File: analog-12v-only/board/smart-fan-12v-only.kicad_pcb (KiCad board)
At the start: 2 copper layers, 62.2 x 41.3 mm, 30 parts, among them J1 KTY81/120, J2 12V_PWR, J3 12V_In, J4 FAN_Out, J5 FAN_Out, Q1 2N3904, Q2 FQP27P06, U1 LM358, U3 NE555P

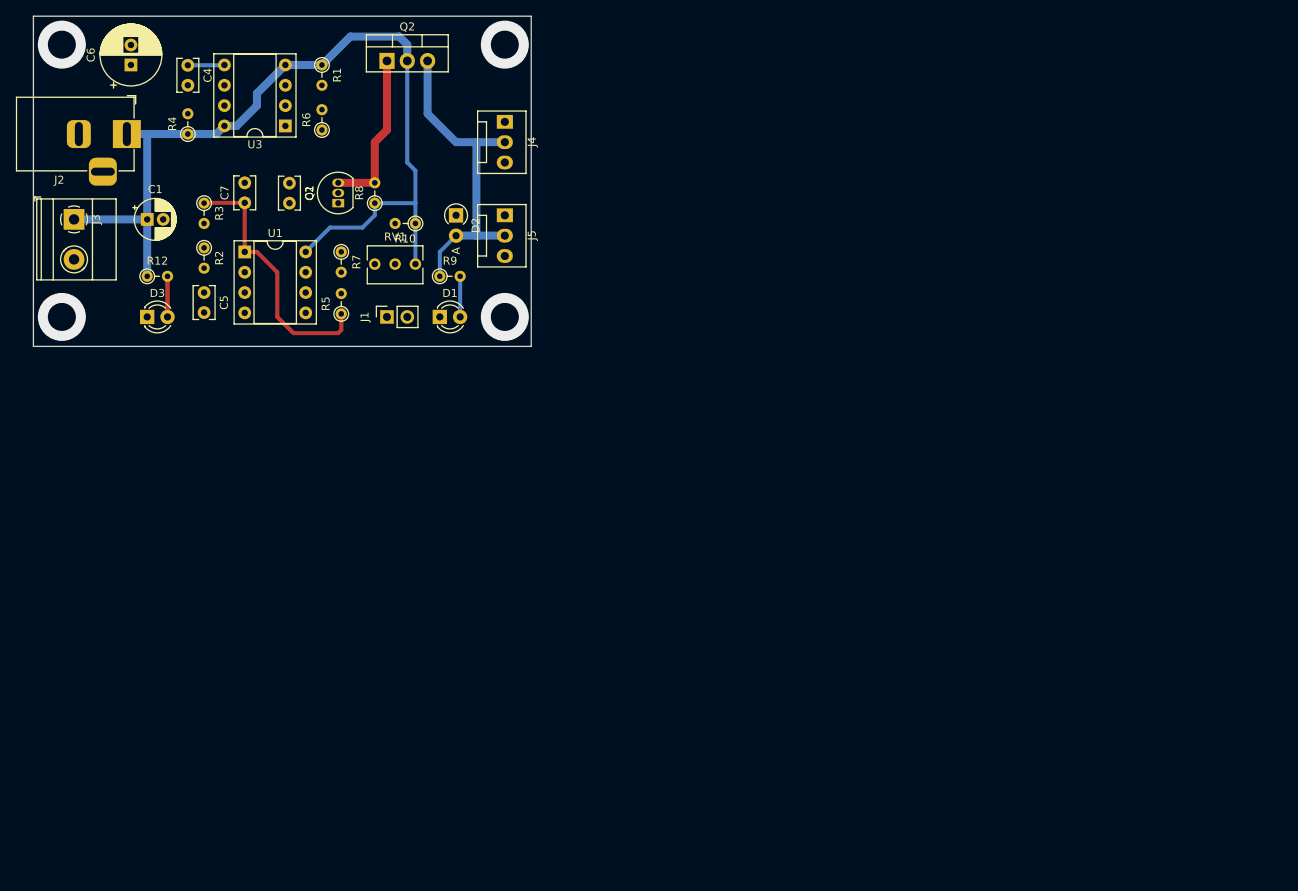
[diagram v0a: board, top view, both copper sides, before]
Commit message: Fix up 12v only analog fan controller
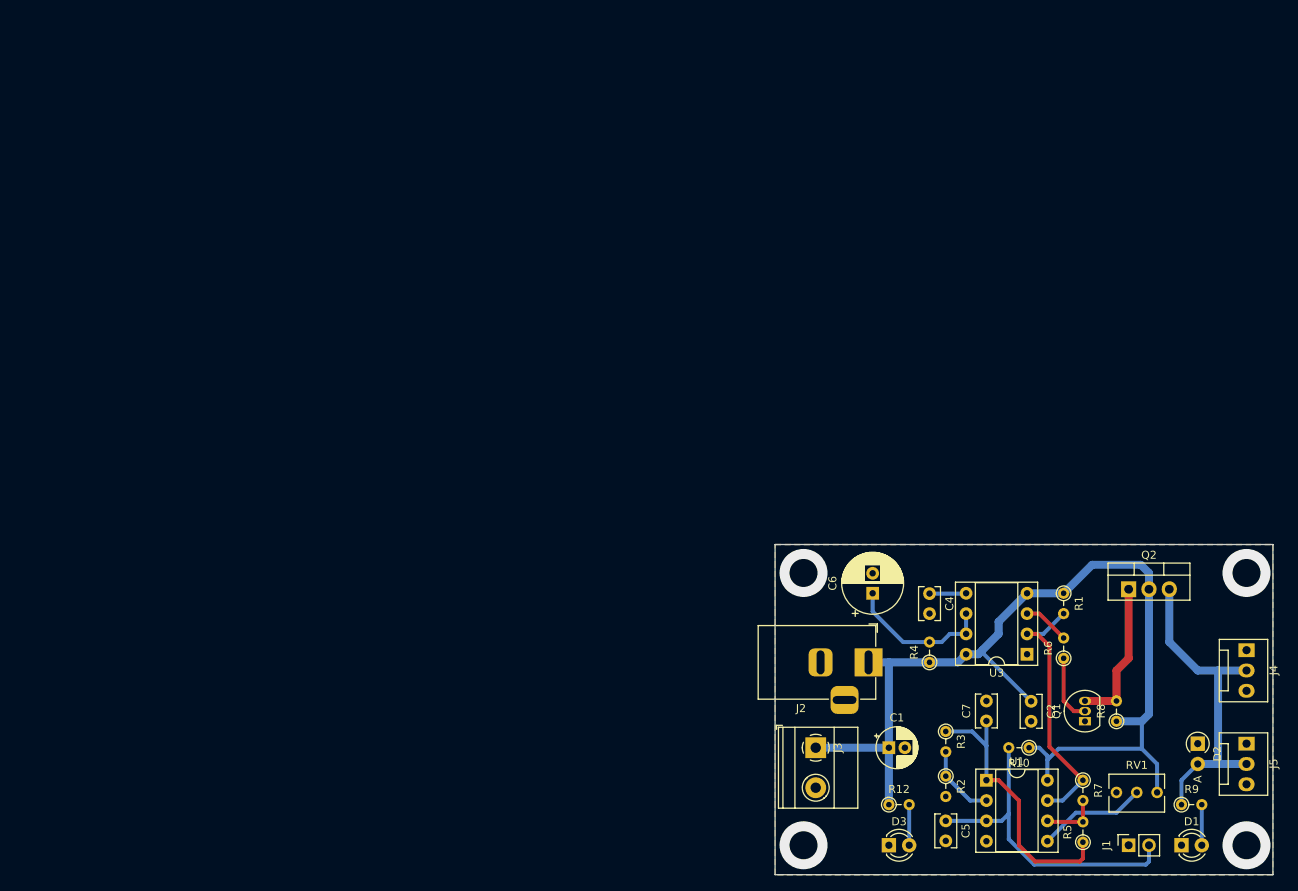
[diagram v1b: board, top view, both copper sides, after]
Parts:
- moved C1 113.8 mm to (118.9, 103.4)
- moved C6 113.8 mm to (116.8, 84.1)
- moved D1 113.8 mm to (155.4, 115.6)
- moved D3 113.8 mm to (118.9, 115.6)
- moved R1 113.8 mm to (140.7, 84.1)
- moved R12 113.8 mm to (118.9, 110.5)
- moved R6 113.8 mm to (140.7, 92.2)
- moved R9 113.8 mm to (155.4, 110.5)
- moved RV1 113.8 mm to (152.4, 109.0)
- moved U3 113.8 mm to (136.1, 91.7)
- moved C4 113.8 mm to (124.0, 84.1)
- moved C5 113.8 mm to (126.0, 112.5)
- moved D2 113.8 mm to (157.5, 102.9)
- moved J1 113.8 mm to (148.8, 115.6)
- moved J2 113.8 mm to (116.3, 92.7)
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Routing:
- net /TMP_IN: track 0.00 -> 40.7 mm
- net Trigger: track 0.00 -> 33.0 mm
- net Net-(C6-Pad1): track 0.00 -> 18.5 mm
- net +12V: track 113.3 -> 127.2 mm
- net Net-(RV1-Pad2): track 0.00 -> 13.7 mm
- net Net-(R2-Pad1): track 0.00 -> 9.39 mm
- net Net-(Q1-Pad2): track 0.00 -> 7.89 mm
- net Net-(R5-Pad2): track 0.00 -> 7.16 mm
- net Net-(R6-Pad2): track 0.00 -> 5.83 mm
- net Net-(C7-Pad1): track 33.0 -> 35.0 mm
- net Net-(Q1-Pad3): track 20.4 -> 18.7 mm
- added copper zone on B.Cu, net GND
- added copper zone on F.Cu, net GND

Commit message: Layout fixes and stable power
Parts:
- removed R6: 2.2k, Resistor_THT:R_Axial_DIN0204_L3.6mm_D1.6mm_P2.54mm_Vertical
- added C3: 10uF, Capacitor_THT:CP_Radial_D5.0mm_P2.00mm, F.Cu at (147.6, 97.9)
- added U2: L7809, Package_TO_SOT_THT:TO-92, F.Cu at (152.1, 98.2)
- D2: value D_Schottky -> 1N5818
- Q1: value 2N3904 -> 2N7000
- R2: value 9.2k -> 1k5
- R3: value 82k -> 3k
- R5: value 2.2k -> 1k
- R7: value 2.2k -> 100k
- R8: value 68k -> 10k
- RV1: value 100k -> 10k
- moved RV1 5.33 mm to (147.1, 109.0), turned to 180 degrees
- moved Q1 4.84 mm to (138.9, 98.2), turned to 0 degrees
- moved R8 4.07 mm to (144.8, 103.3), turned to 180 degrees
- moved R3 3.18 mm to (128.5, 103.3), turned to 180 degrees
- moved C7 2.74 mm to (128.5, 99.0)
- moved C2 2.74 mm to (134.1, 96.6)
- moved Q2 0.51 mm to (149.4, 83.6)
- moved R10 0.13 mm to (136.4, 103.3)
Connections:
- C2 pad 1: +12V -> +9V
- R1 pad 1: +12V -> +9V
- R10 pad 1: +12V -> +9V
- R4 pad 1: +12V -> +9V
- RV1 pad 1: +12V -> +9V
- U1 pad 8: +12V -> +9V
- U3 pad 3: Net-(R6-Pad2) -> Net-(Q1-Pad2)
- U3 pad 4: +12V -> +9V
- U3 pad 8: +12V -> +9V
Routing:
- net +9V: track 0.00 -> 78.5 mm
- net +12V: track 127.2 -> 103.8 mm
- net Net-(Q1-Pad2): track 7.89 -> 13.9 mm
- net Net-(R6-Pad2): track 5.83 -> 0.00 mm
- net Net-(Q1-Pad3): track 18.7 -> 23.3 mm
- net Net-(C7-Pad1): track 35.0 -> 31.2 mm
- net Trigger: track 33.0 -> 35.0 mm
- net Net-(D2-Pad2): track 41.4 -> 40.9 mm

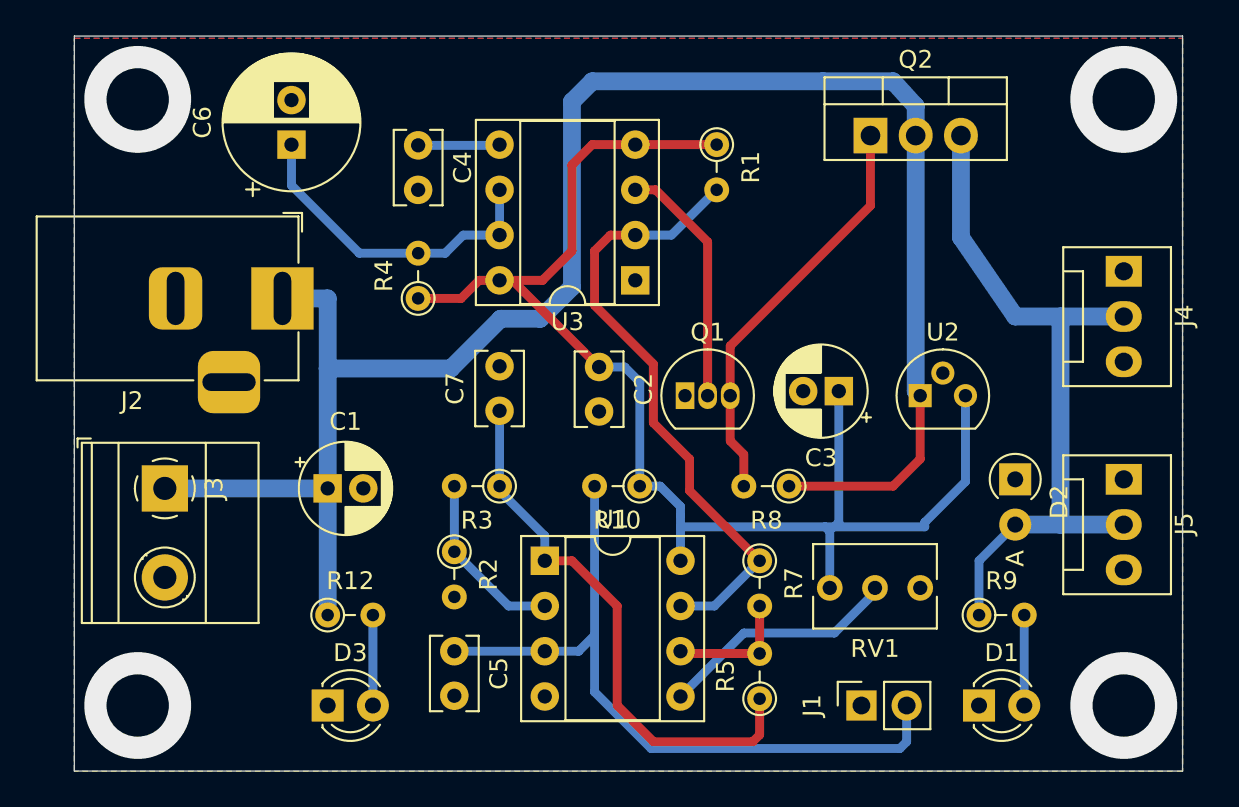
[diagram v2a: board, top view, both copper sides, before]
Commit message: Fix board layout
Power transistor drain-source swapped
Flyback diode reversed
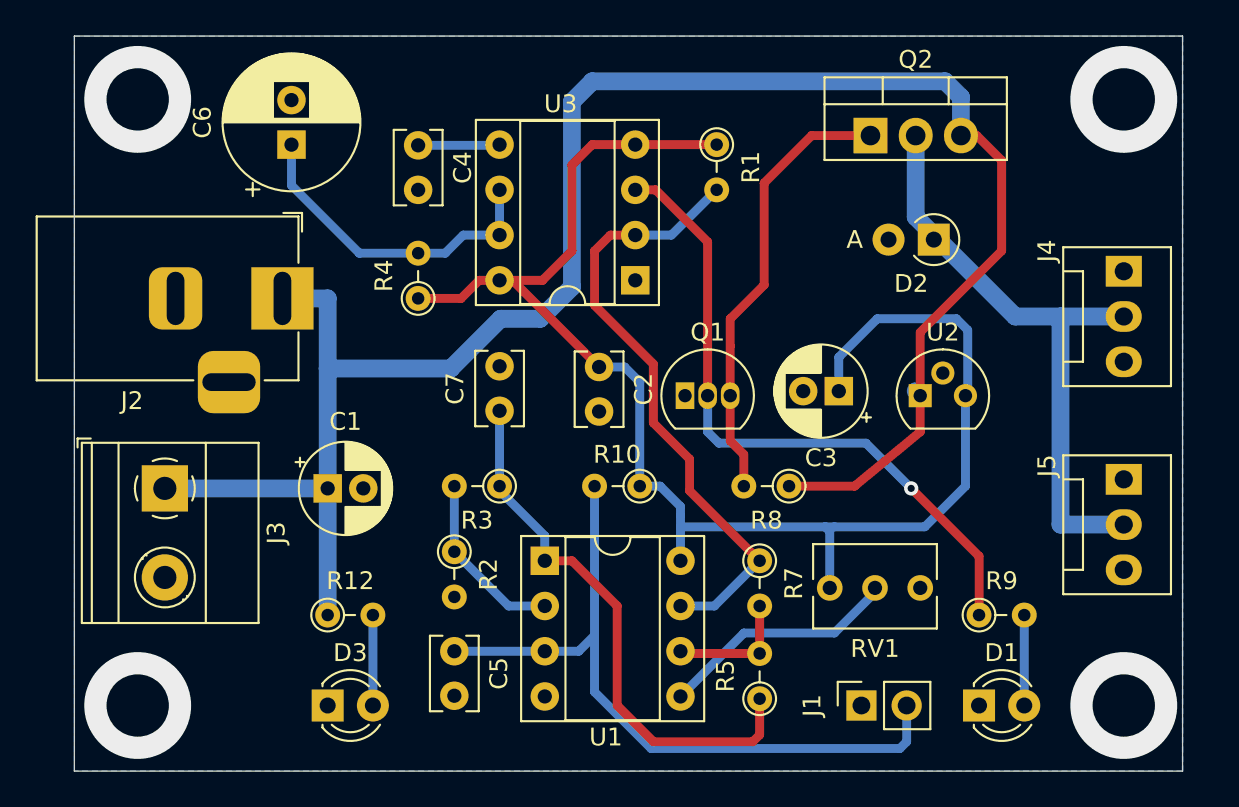
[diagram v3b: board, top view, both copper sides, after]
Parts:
- C6: value 100uF -> 330uF
- D2: value 1N5818 -> 1N5820
- R1: value 1M -> 100k
- R12: value 27k -> 5k
- R4: value 100k -> 1M
- R9: value 27k -> 3k3
- moved D2 14.2 mm to (152.9, 89.4), turned to 180 degrees
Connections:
- D2 pad 1: GND -> Net-(D2-Pad1)
- D2 pad 2: Net-(D2-Pad2) -> GND
- J4 pad 2: Net-(D2-Pad2) -> Net-(D2-Pad1)
- J5 pad 2: Net-(D2-Pad2) -> Net-(D2-Pad1)
- Q2 pad 2: +12V -> Net-(D2-Pad1)
- Q2 pad 3: Net-(D2-Pad2) -> +12V
- R9 pad 1: Net-(D2-Pad2) -> Net-(Q1-Pad2)
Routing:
- net Net-(D2-Pad2): track 40.9 -> 0.00 mm
- net Net-(D2-Pad1): track 0.00 -> 33.8 mm
- net Net-(Q1-Pad2): track 13.9 -> 37.4 mm, vias 0 -> 1
- net +9V: track 78.5 -> 84.8 mm
- net +12V: track 103.8 -> 109.2 mm
- net Net-(Q1-Pad3): track 23.3 -> 25.2 mm
- removed copper zone on F.Cu, net GND

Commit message: WIP: Cleaning up board
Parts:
- removed R10: 10k, Resistor_THT:R_Axial_DIN0204_L3.6mm_D1.6mm_P2.54mm_Vertical
- J1: value KTY81/120 -> Conn_01x03_Female; footprint Connector_Pin254mm:PinSocket_1x02_P2.54mm_Vertical -> Connector_PinSocket_2.54mm:PinSocket_1x03_P2.54mm_Vertical
- Q2: footprint Package_TO_SOT_THT:TO-220-3_Vertical -> Package_TO_SOT_THT:TO-251-3-1EP_Horizontal_TabDown
- R2: value 1k5 -> 10k
- R3: value 3k -> 10k
- U1: value LM358 -> L78L05_TO92; footprint Package_DIP:DIP-8_W7.62mm_Socket -> Package_TO_SOT_THT:TO-92_Inline
- U2: value L7809 -> LM555; footprint Package_TO_SOT_THT:TO-92 -> Package_DIP:DIP-8_W7.62mm_Socket
- U3: value NE555P -> MCP602
- moved U1 25.5 mm to (154.7, 97.9), turned to 180 degrees
- moved U2 17.2 mm to (136.1, 91.8), turned to 180 degrees
- moved U3 16.5 mm to (131.1, 107.4), turned to 0 degrees
- moved Q2 4.05 mm to (146.7, 80.5), turned to 270 degrees
- moved D2 3.59 mm to (156.0, 91.3)
- moved J1 3.05 mm to (151.9, 115.6), turned to 270 degrees
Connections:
- C2 pad 1: +9V -> +5V
- C3 pad 1: +9V -> +5V
- R1 pad 1: +9V -> +5V
- R4 pad 1: +9V -> +5V
- RV1 pad 1: +9V -> +5V
- U1 pad 1: Net-(C7-Pad1) -> +5V
- U1 pad 2: Net-(R2-Pad1) -> GND
- U1 pad 3: /TMP_IN -> +12V
- U2 pad 1: +12V -> GND
- U2 pad 2: GND -> Trigger
- U2 pad 3: +9V -> Net-(Q1-Pad2)
- U3 pad 1: GND -> Net-(C7-Pad1)
- U3 pad 2: Trigger -> Net-(R2-Pad1)
- U3 pad 3: Net-(Q1-Pad2) -> /TMP_IN
- U3 pad 4: +9V -> GND
- U3 pad 5: Net-(C4-Pad1) -> Net-(RV1-Pad2)
- U3 pad 6: Net-(C6-Pad1) -> Net-(R5-Pad2)
- U3 pad 7: Net-(C6-Pad1) -> Trigger
- U3 pad 8: +9V -> +5V
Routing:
- net +5V: track 0.00 -> 90.7 mm
- net +9V: track 84.8 -> 0.00 mm
- net +12V: track 109.2 -> 67.6 mm
- net Net-(Q1-Pad3): track 25.2 -> 9.71 mm
- net Net-(D2-Pad1): track 33.8 -> 18.8 mm
- net /TMP_IN: track 40.7 -> 28.1 mm
- net (no net): vias 4 -> 34
- added copper zone on B.Cu, net (none)
- added copper zone on F.Cu, net (none)
- removed copper zone on B.Cu, net GND
